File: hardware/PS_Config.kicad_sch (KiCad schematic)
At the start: 16 parts, among them J3 Micro_SD_Card, SW2 SW_DIP_x01, U2 xc7z020clg400, X2 ECS-2520MV-xxx-xx

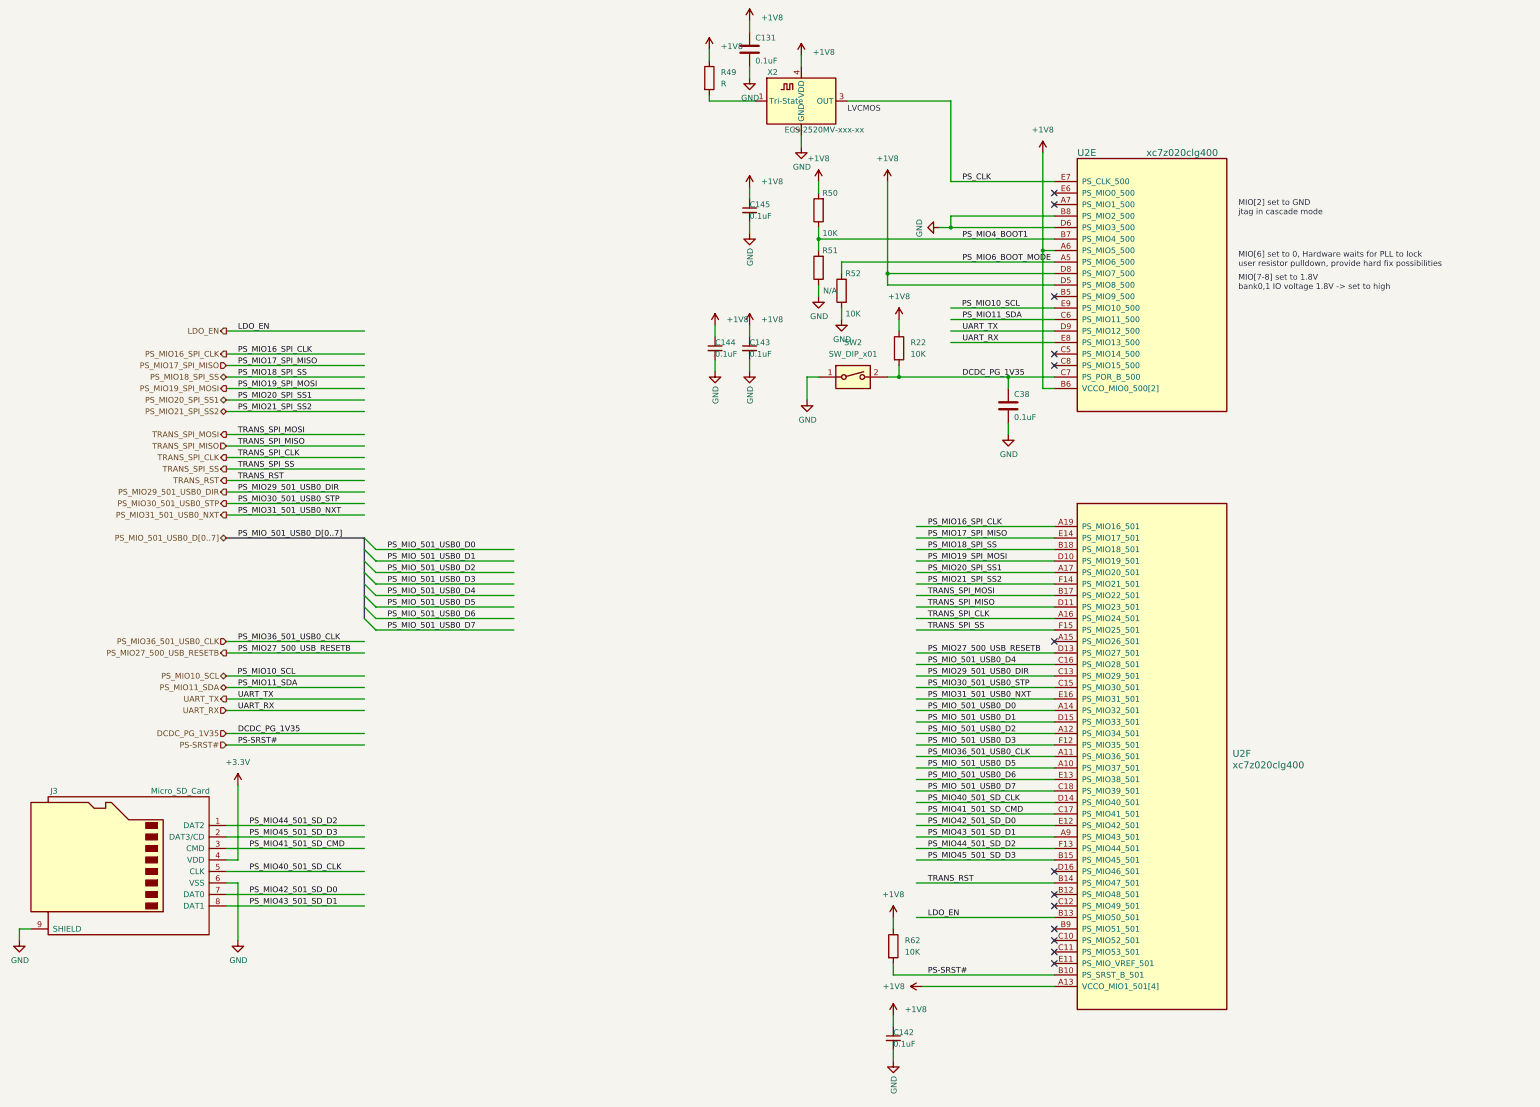
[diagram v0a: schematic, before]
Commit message: add sdio level shift ciruit
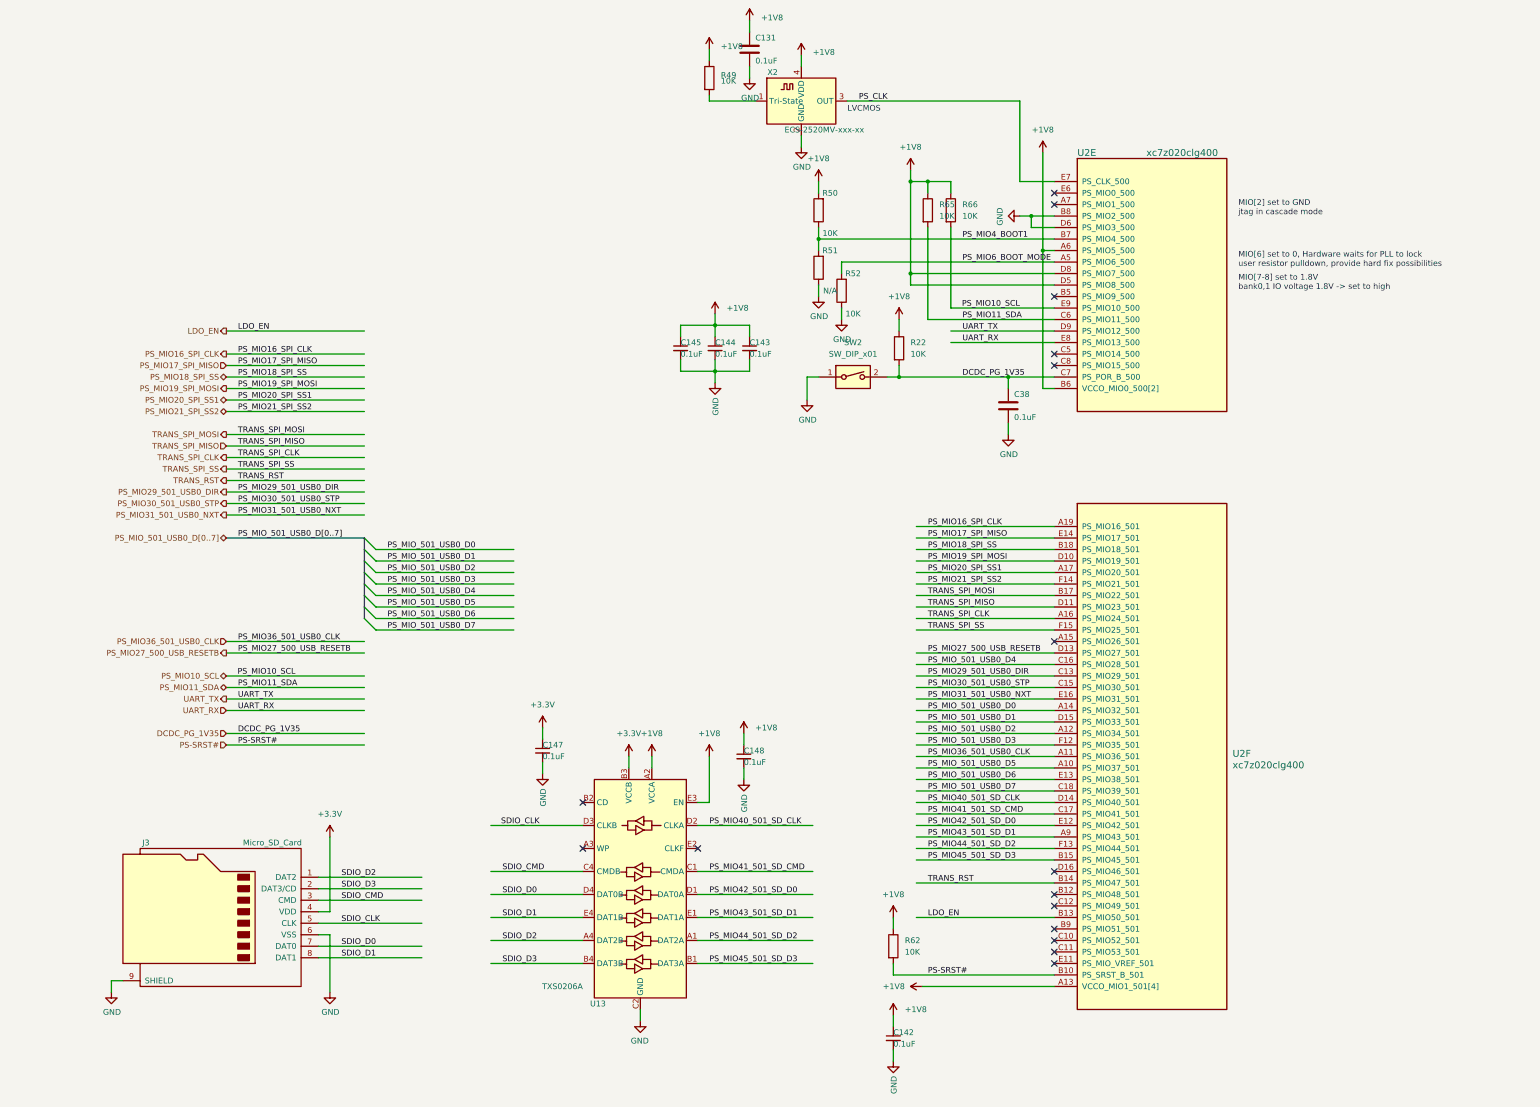
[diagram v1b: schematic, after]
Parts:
- added C147, C148: 0.1uF, Capacitor_SMD:C_0201_0603Metric, symbol Device:C_Small
- added R65, R66: 10K, Resistor_SMD:R_0201_0603Metric, symbol Device:R
- added U13: TXS0206A, Package_CSP_Local:WLCSP-20_1.609x1.994mm_Layout4x5_P0.4mm, symbol Logic LevelTransistor_Local:TXS0206A
- R49: value R -> 10K
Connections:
- net +1V8: now also C148.1, R65.1, R66.1, U13.A2 (VCCA), U13.E3 (EN)
- net +3V3: now also C147.1, U13.B3 (VCCB)
- net GND: now also C147.2, C148.2, U13.C2 (GND), U13.C3 (GND)
- net PS_MIO10_SCL: now also R66.2
- net PS_MIO11_SDA: now also R65.2
- net PS_MIO40_501_SD_CLK: now also U13.D2 (CLKA); no longer J3.5 (CLK)
- net PS_MIO41_501_SD_CMD: now also U13.C1 (CMDA); no longer J3.3 (CMD)
- net PS_MIO42_501_SD_D0: now also U13.D1 (DAT0A); no longer J3.7 (DAT0)
- net PS_MIO43_501_SD_D1: now also U13.E1 (DAT1A); no longer J3.8 (DAT1)
- net PS_MIO44_501_SD_D2: now also U13.A1 (DAT2A); no longer J3.1 (DAT2)
- net PS_MIO45_501_SD_D3: now also U13.B1 (DAT3A); no longer J3.2 (DAT3/CD)
- new net SDIO_CLK: J3.5 (CLK), U13.D3 (CLKB)
- new net SDIO_CMD: J3.3 (CMD), U13.C4 (CMDB)
- new net SDIO_D0: J3.7 (DAT0), U13.D4 (DAT0B)
- new net SDIO_D1: J3.8 (DAT1), U13.E4 (DAT1B)
- new net SDIO_D2: J3.1 (DAT2), U13.A4 (DAT2B)
- new net SDIO_D3: J3.2 (DAT3/CD), U13.B4 (DAT3B)
- no-connect marks 13 -> 16
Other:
- moved on the sheet: C145, J3

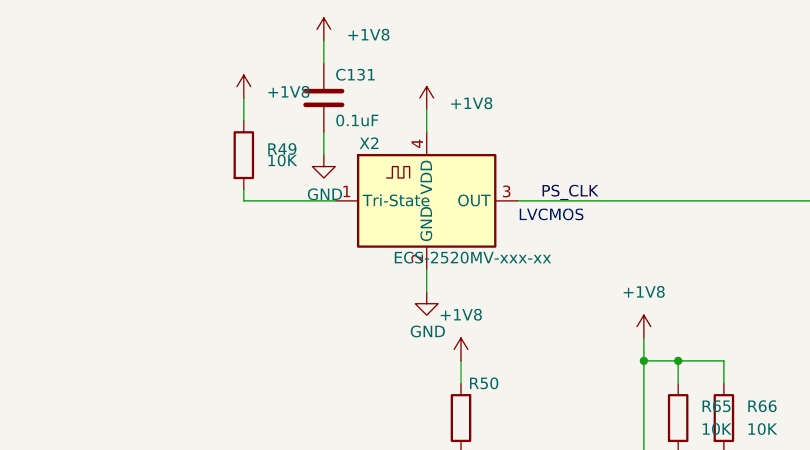
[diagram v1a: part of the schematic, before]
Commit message: Add PS I2C pullup resistor
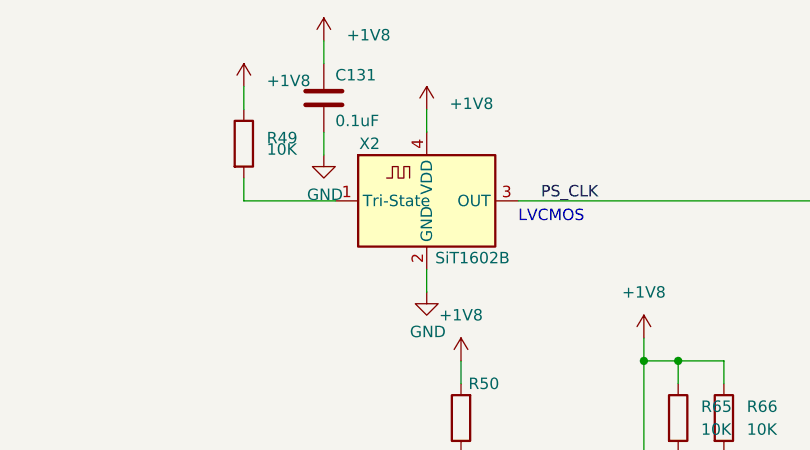
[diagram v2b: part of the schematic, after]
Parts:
- X2: value ECS-2520MV-xxx-xx -> SiT1602B
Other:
- moved on the sheet: R49
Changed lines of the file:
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@@
     (stroke (width 0) (type default))
   )
-  (wire (pts (xy 208.28 31.75) (xy 208.28 34.29))
+  (wire (pts (xy 208.28 30.48) (xy 208.28 33.02))
     (stroke (width 0) (type default))
   )
@@
     (stroke (width 0) (type default))
   )
-  (wire (pts (xy 208.28 43.18) (xy 208.28 41.91))
+  (wire (pts (xy 208.28 43.18) (xy 208.28 40.64))
     (stroke (width 0) (type default))
   )
@@
     (pin "1")
   )
-  (symbol (lib_id "Device:R") (at 208.28 38.1 0) (unit 1)
-    (in_bom yes) (on_board yes) (fields_autoplaced)
-    (property "Reference" "R49" (id 0) (at 210.82 37.465 0)
-      (effects (font (size 1.27 1.27)) (justify left))
-    )
-    (property "Value" "10K" (id 1) (at 210.82 38.735 0)
-      (effects (font (size 1.27 1.27)) (justify left))
-    )
-    (property "Footprint" "Resistor_SMD:R_0201_0603Metric" (id 2) (at 206.502 38.1 90)
-      (effects (font (size 1.27 1.27)) hide)
-    )
-    (property "Datasheet" "~" (id 3) (at 208.28 38.1 0)
+  (symbol (lib_id "Device:R") (at 208.28 36.83 0) (unit 1)
+    (in_bom yes) (on_board yes) (fields_autoplaced)
+    (property "Reference" "R49" (id 0) (at 210.82 36.195 0)
+      (effects (font (size 1.27 1.27)) (justify left))
+    )
+    (property "Value" "10K" (id 1) (at 210.82 37.465 0)
+      (effects (font (size 1.27 1.27)) (justify left))
+    )
+    (property "Footprint" "Resistor_SMD:R_0201_0603Metric" (id 2) (at 206.502 36.83 90)
+      (effects (font (size 1.27 1.27)) hide)
+    )
+    (property "Datasheet" "~" (id 3) (at 208.28 36.83 0)
       (effects (font (size 1.27 1.27)) hide)
     )
@@
     (pin "1")
   )
-  (symbol (lib_id "power:+1V8") (at 208.28 31.75 0) (unit 1)
-    (in_bom yes) (on_board yes) (fields_autoplaced)
-    (property "Reference" "#PWR0201" (id 0) (at 208.28 35.56 0)
-      (effects (font (size 1.27 1.27)) hide)
-    )
-    (property "Value" "+1V8" (id 1) (at 210.82 31.115 0)
-      (effects (font (size 1.27 1.27)) (justify left))
-    )
-    (property "Footprint" "" (id 2) (at 208.28 31.75 0)
-      (effects (font (size 1.27 1.27)) hide)
-    )
-    (property "Datasheet" "" (id 3) (at 208.28 31.75 0)
+  (symbol (lib_id "power:+1V8") (at 208.28 30.48 0) (unit 1)
+    (in_bom yes) (on_board yes) (fields_autoplaced)
+    (property "Reference" "#PWR0201" (id 0) (at 208.28 34.29 0)
+      (effects (font (size 1.27 1.27)) hide)
+    )
+    (property "Value" "+1V8" (id 1) (at 210.82 29.845 0)
+      (effects (font (size 1.27 1.27)) (justify left))
+    )
+    (property "Footprint" "" (id 2) (at 208.28 30.48 0)
+      (effects (font (size 1.27 1.27)) hide)
+    )
+    (property "Datasheet" "" (id 3) (at 208.28 30.48 0)
       (effects (font (size 1.27 1.27)) hide)
     )
@@
       (effects (font (size 1.27 1.27)))
     )
-    (property "Value" "ECS-2520MV-xxx-xx" (id 1) (at 233.68 49.53 0)
-      (effects (font (size 1.27 1.27)))
-    )
+    (property "Value" "SiT1602B" (id 1) (at 233.68 49.53 0)
+      (effects (font (size 1.27 1.27)))
+    )

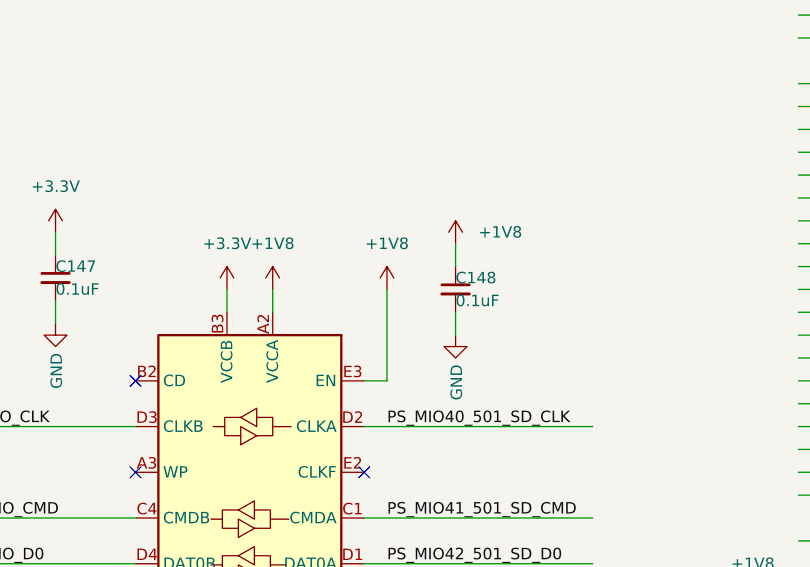
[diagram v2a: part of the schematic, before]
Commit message: Modify wrong DCDC TPS62088 package Panelize PCB Add manufacture requirements files
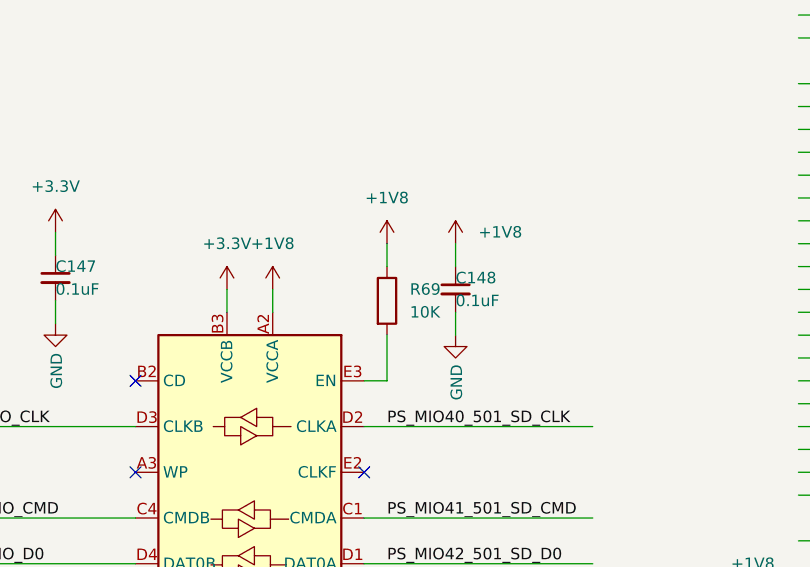
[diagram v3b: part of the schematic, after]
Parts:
- added R69: 10K, Resistor_SMD:R_0201_0603Metric, symbol Device:R
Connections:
- net +1V8: now also R69.1; no longer U13.E3 (EN)
- new net: R69.2, U13.E3 (EN)
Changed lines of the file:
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@@
+    (stroke (width 0) (type default))
+  )
+  (wire (pts (xy 208.28 193.04) (xy 208.28 198.12))
     (stroke (width 0) (type default))
   )
@@
     (stroke (width 0) (type default))
   )
-  (wire (pts (xy 208.28 187.96) (xy 208.28 198.12))
+  (wire (pts (xy 208.28 182.88) (xy 208.28 185.42))
     (stroke (width 0) (type default))
   )
@@
     (effects (font (size 1.27 1.27)) (justify right))
   )
-  (symbol (lib_id "power:+1V8") (at 208.28 187.96 0) (mirror y) (unit 1)
-    (in_bom yes) (on_board yes) (fields_autoplaced)
-    (property "Reference" "#PWR0279" (id 0) (at 208.28 191.77 0)
-      (effects (font (size 1.27 1.27)) hide)
-    )
-    (property "Value" "+1V8" (id 1) (at 208.28 182.88 0)
-      (effects (font (size 1.27 1.27)))
-    )
-    (property "Footprint" "" (id 2) (at 208.28 187.96 0)
-      (effects (font (size 1.27 1.27)) hide)
-    )
-    (property "Datasheet" "" (id 3) (at 208.28 187.96 0)
+  (symbol (lib_id "power:+1V8") (at 208.28 182.88 0) (mirror y) (unit 1)
+    (in_bom yes) (on_board yes) (fields_autoplaced)
+    (property "Reference" "#PWR0279" (id 0) (at 208.28 186.69 0)
+      (effects (font (size 1.27 1.27)) hide)
+    )
+    (property "Value" "+1V8" (id 1) (at 208.28 177.8 0)
+      (effects (font (size 1.27 1.27)))
+    )
+    (property "Footprint" "" (id 2) (at 208.28 182.88 0)
+      (effects (font (size 1.27 1.27)) hide)
+    )
+    (property "Datasheet" "" (id 3) (at 208.28 182.88 0)
       (effects (font (size 1.27 1.27)) hide)
     )
@@
     (pin "E9")
   )
+  (symbol (lib_id "Device:R") (at 208.28 189.23 0) (unit 1)
+    (in_bom yes) (on_board yes) (fields_autoplaced)
+    (property "Reference" "R69" (id 0) (at 210.82 187.9599 0)
+      (effects (font (size 1.27 1.27)) (justify left))
+    )
+    (property "Value" "10K" (id 1) (at 210.82 190.4999 0)
+      (effects (font (size 1.27 1.27)) (justify left))
+    )
+    (property "Footprint" "Resistor_SMD:R_0201_0603Metric" (id 2) (at 206.502 189.23 90)
+      (effects (font (size 1.27 1.27)) hide)
+    )
+    (property "Datasheet" "~" (id 3) (at 208.28 189.23 0)
+      (effects (font (size 1.27 1.27)) hide)
+    )
+    (pin "1")
+    (pin "2")
+  )
   (symbol (lib_id "Device:C_Small") (at 201.93 97.79 0) (unit 1)
